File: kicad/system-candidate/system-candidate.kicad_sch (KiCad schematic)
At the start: 217 parts, among them J1 691137710002 2P 5.00mm, J2 Auxiliary 12V, J3 Differential audio, J301 T1_SECONDARY, J4 Control 2x4: 3V3 RESET FAULT 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, J401 START_BUTTON, J5 B2P-VH(LF)(SN), J6 GND braid solder bond - NO mo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, J7 B7B-XH-A(LF)(SN), K501 G6K-2F DC12, Q501 MMBT3904, Q502 MMBT3904, Q601 BCP56, Q602 BCP53, Q603 BSS138, U1 TPA3255DDV, U2 OPA1656ID, U3 OPA1656ID, U302 LM5164DDA, U303 TPS3700DDC, U401 LP2985-33, U402 TPS3808G33, U403 TPS3808G33, U404 TPS3808G33, U405 74LVC1G14, U406 74LVC2G74, U407 74LVC2G74, U408 74LVC1G32, U409 74LVC1G07, U410 74LVC1G08, U411 74LVC1G06, U412 TPS3700DDC, U413 TPS3700DDC, U414 TPS3808G33, U415 74LVC1G08, U416 TPS3808G33, U417 74LVC2G74, U418 74LVC1G32, U419 74LVC1G07, U501 TPS3700DDC, U502 TPS3700DDC, U503 TMUX6219, U504 TPS3700DDC

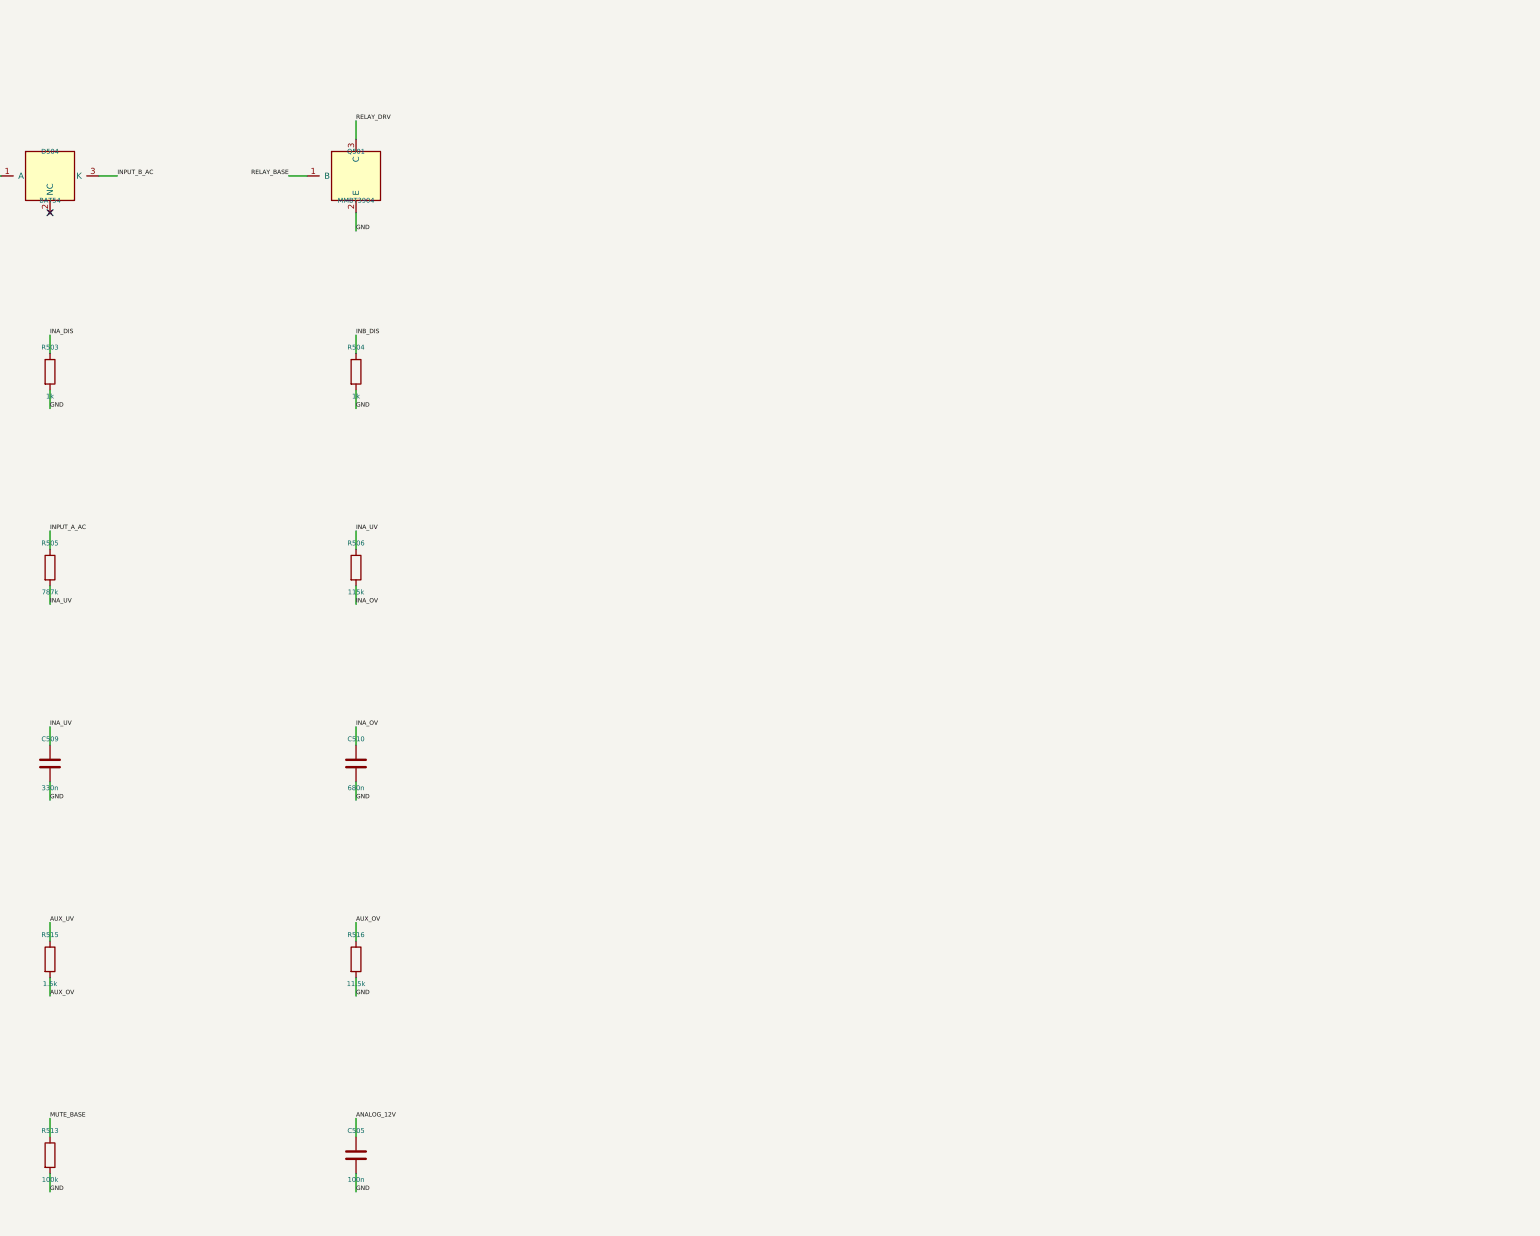
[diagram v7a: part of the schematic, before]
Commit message: feat(pcb): test points, LEDs de status, saída de fan e nova rota (PCB-004)
- 21 test points com nome no silk (SPK± fora), 6 LEDs: PVDD, RAILS_OK, RUN,
  AUDIO, FAULT, CLIP_OTW, só via gates de MOSFET
- fan 12 V em J8 com AO3400A, flyback e jumper de modo (sempre/CLIP_OTW)
- re-rota: 2.973 trilhas, 404 vias; ERC 0, paridade 0; 59 conexões abertas
  e 3 starved_thermal; removidos trechos PVDD/T1_A com isolamento 0,118 mm
- docs/bringup.md com valores esperados por test point; PCB-001/PCB-004 Done
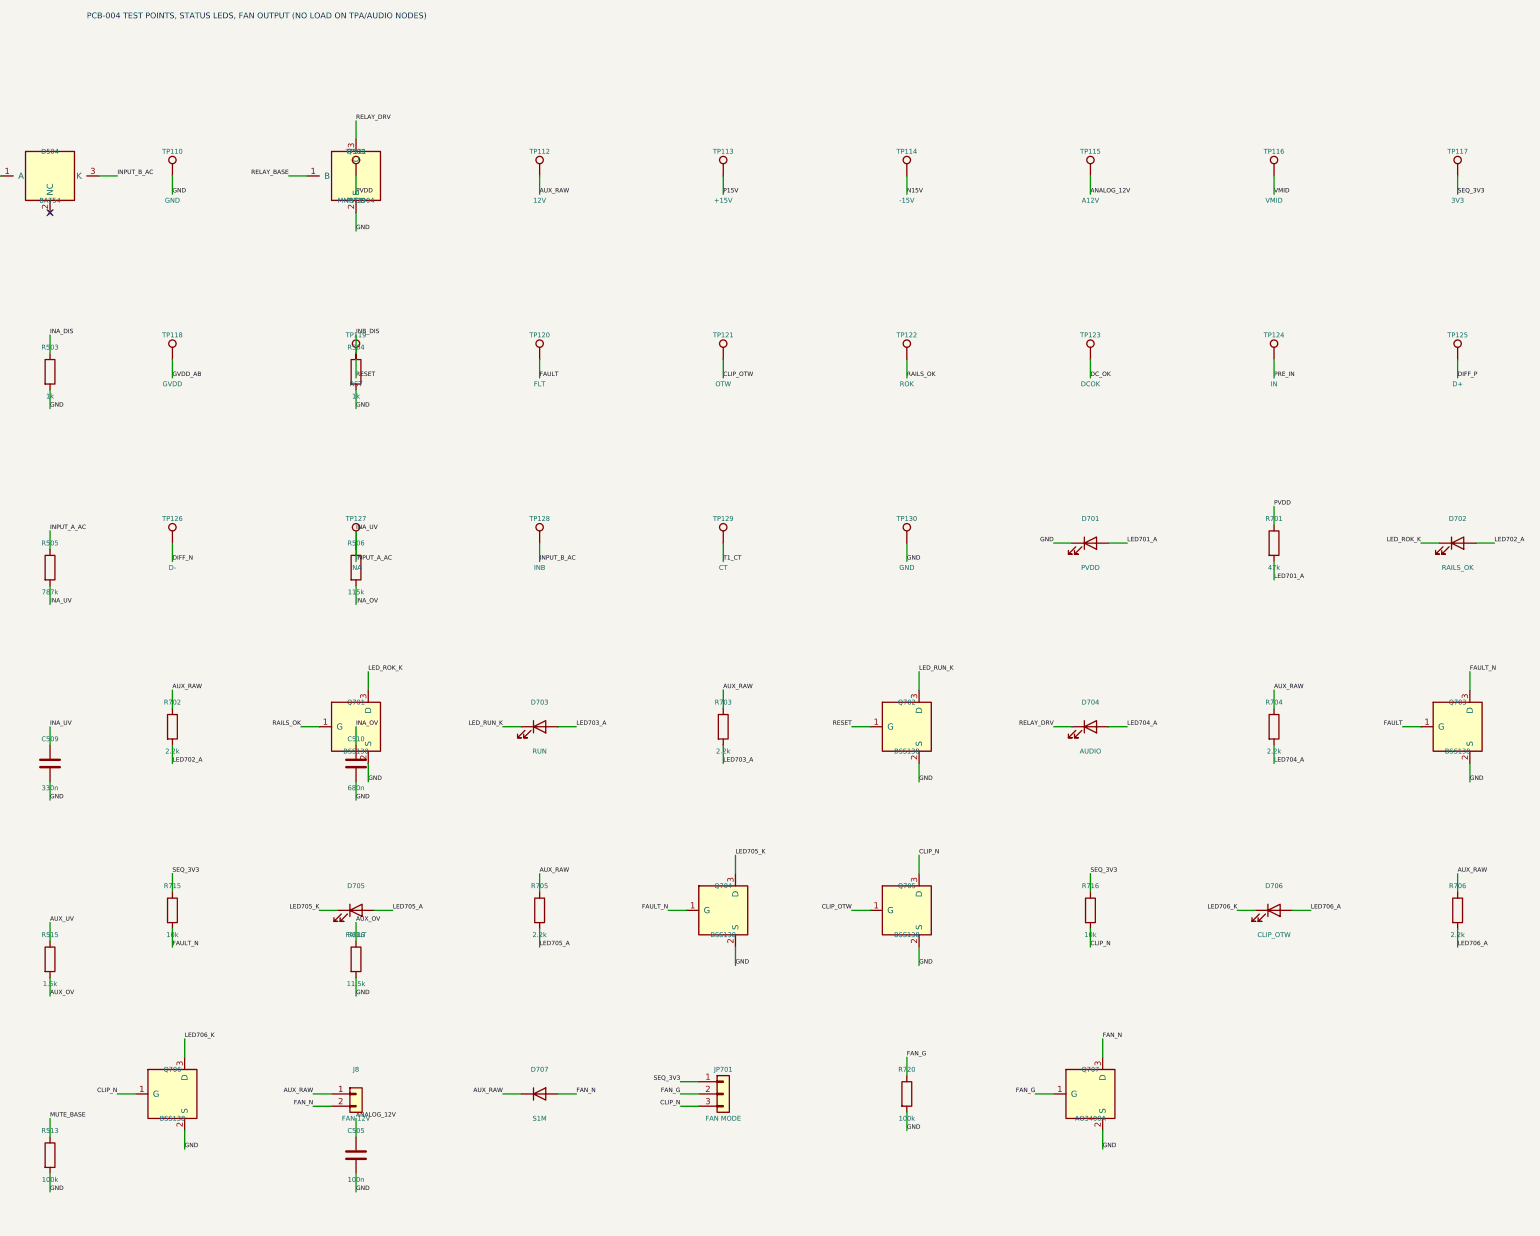
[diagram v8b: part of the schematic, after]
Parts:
- added D701: PVDD, LED_SMD:LED_0805_2012Metric, symbol Device:LED
- added D702: RAILS_OK, LED_SMD:LED_0805_2012Metric, symbol Device:LED
- added D703: RUN, LED_SMD:LED_0805_2012Metric, symbol Device:LED
- added D704: AUDIO, LED_SMD:LED_0805_2012Metric, symbol Device:LED
- added D705: FAULT, LED_SMD:LED_0805_2012Metric, symbol Device:LED
- added D706: CLIP_OTW, LED_SMD:LED_0805_2012Metric, symbol Device:LED
- added D707: S1M, Diode_SMD:D_SMA, symbol Device:D
- added J8: FAN 12V, Connector_JST:JST_XH_B2B-XH-A_1x02_P2.50mm_Vertical, symbol Connector_Generic:Conn_01x02
- added JP701: FAN MODE, Connector_PinHeader_2.54mm:PinHeader_1x03_P2.54mm_Vertical, symbol Connector_Generic:Conn_01x03
- added Q701, Q702, Q703, Q704, Q705, Q706: BSS138, Package_TO_SOT_SMD:SOT-23, symbol PS28_PRE:BSS138
- added Q707: AO3400A, Package_TO_SOT_SMD:SOT-23, symbol PS28_PRE:AO3400A
- added R701: 47k, Resistor_SMD:R_1206_3216Metric, symbol Device:R
- added R702, R703, R704, R705, R706: 2.2k, Resistor_SMD:R_0805_2012Metric, symbol Device:R
- added R715, R716: 10k, Resistor_SMD:R_0805_2012Metric, symbol Device:R
- added R720: 100k, Resistor_SMD:R_0805_2012Metric, symbol Device:R
- added TP110, TP130: GND, TestPoint:TestPoint_Pad_D2.0mm, symbol Connector:TestPoint
- added TP111: PVDD, TestPoint:TestPoint_Pad_D2.0mm, symbol Connector:TestPoint
- added TP112: 12V, TestPoint:TestPoint_Pad_D2.0mm, symbol Connector:TestPoint
- added TP113: +15V, TestPoint:TestPoint_Pad_D2.0mm, symbol Connector:TestPoint
- added TP114: -15V, TestPoint:TestPoint_Pad_D2.0mm, symbol Connector:TestPoint
- added TP115: A12V, TestPoint:TestPoint_Pad_D2.0mm, symbol Connector:TestPoint
- added TP116: VMID, TestPoint:TestPoint_Pad_D2.0mm, symbol Connector:TestPoint
- added TP117: 3V3, TestPoint:TestPoint_Pad_D2.0mm, symbol Connector:TestPoint
- added TP118: GVDD, TestPoint:TestPoint_Pad_D2.0mm, symbol Connector:TestPoint
- added TP119: RST, TestPoint:TestPoint_Pad_D2.0mm, symbol Connector:TestPoint
- added TP120: FLT, TestPoint:TestPoint_Pad_D2.0mm, symbol Connector:TestPoint
- added TP121: OTW, TestPoint:TestPoint_Pad_D2.0mm, symbol Connector:TestPoint
- added TP122: ROK, TestPoint:TestPoint_Pad_D2.0mm, symbol Connector:TestPoint
- added TP123: DCOK, TestPoint:TestPoint_Pad_D2.0mm, symbol Connector:TestPoint
- added TP124: IN, TestPoint:TestPoint_Pad_D2.0mm, symbol Connector:TestPoint
- added TP125: D+, TestPoint:TestPoint_Pad_D2.0mm, symbol Connector:TestPoint
- added TP126: D-, TestPoint:TestPoint_Pad_D2.0mm, symbol Connector:TestPoint
- added TP127: INA, TestPoint:TestPoint_Pad_D2.0mm, symbol Connector:TestPoint
- added TP128: INB, TestPoint:TestPoint_Pad_D2.0mm, symbol Connector:TestPoint
- added TP129: CT, TestPoint:TestPoint_Pad_D2.0mm, symbol Connector:TestPoint
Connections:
- net INPUT_A_AC is gone; now on net INA_UV: C503.1, D503.3 (K), R505.1, R517.2, U1.5 (INPUT_A)
- net ANALOG_12V: now also TP115.1
- net AUX_RAW: now also D707.1 (K), J8.1 (Pin_1), R702.1, R703.1, R704.1, R705.1, R706.1, TP112.1
- net CLIP_OTW: now also Q705.1 (G), TP121.1
- net DC_OK: now also TP123.1
- net DIFF_N: now also TP126.1
- net DIFF_P: now also TP125.1
- net FAULT: now also Q703.1 (G), TP120.1
- net GND: now also D701.1 (K), Q701.2 (S), Q702.2 (S), Q703.2 (S), Q704.2 (S), Q705.2 (S), Q706.2 (S), Q707.2 (S), R720.2, TP110.1, TP130.1
- net GVDD_AB: now also TP118.1
- net INA_UV: now also TP127.1
- net INPUT_B_AC: now also TP128.1
- net N15V: now also TP114.1
- net P15V: now also TP113.1
- net PRE_IN: now also TP124.1
- net PVDD: now also R701.1, TP111.1
- net RAILS_OK: now also Q701.1 (G), TP122.1
- net RELAY_DRV: now also D704.1 (K)
- net RESET: now also Q702.1 (G), TP119.1
- net SEQ_3V3: now also JP701.1 (Pin_1), R715.1, R716.1, TP117.1
- net T1_CT: now also TP129.1
- net VMID: now also TP116.1
- new net CLIP_N: JP701.3 (Pin_3), Q705.3 (D), Q706.1 (G), R716.2
- new net FAN_G: JP701.2 (Pin_2), Q707.1 (G), R720.1
- new net FAN_N: D707.2 (A), J8.2 (Pin_2), Q707.3 (D)
- new net FAULT_N: Q703.3 (D), Q704.1 (G), R715.2
- new net LED701_A: D701.2 (A), R701.2
- new net LED702_A: D702.2 (A), R702.2
- new net LED703_A: D703.2 (A), R703.2
- new net LED704_A: D704.2 (A), R704.2
- new net LED705_A: D705.2 (A), R705.2
- new net LED705_K: D705.1 (K), Q704.3 (D)
- new net LED706_A: D706.2 (A), R706.2
- new net LED706_K: D706.1 (K), Q706.3 (D)
- new net LED_ROK_K: D702.1 (K), Q701.3 (D)
- new net LED_RUN_K: D703.1 (K), Q702.3 (D)
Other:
- note added: "PCB-004 TEST POINTS, STATUS LEDS, FAN OUTPUT (NO LOAD ON TPA/AUDIO NODES)"
